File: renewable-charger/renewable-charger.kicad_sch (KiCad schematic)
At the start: 19 parts

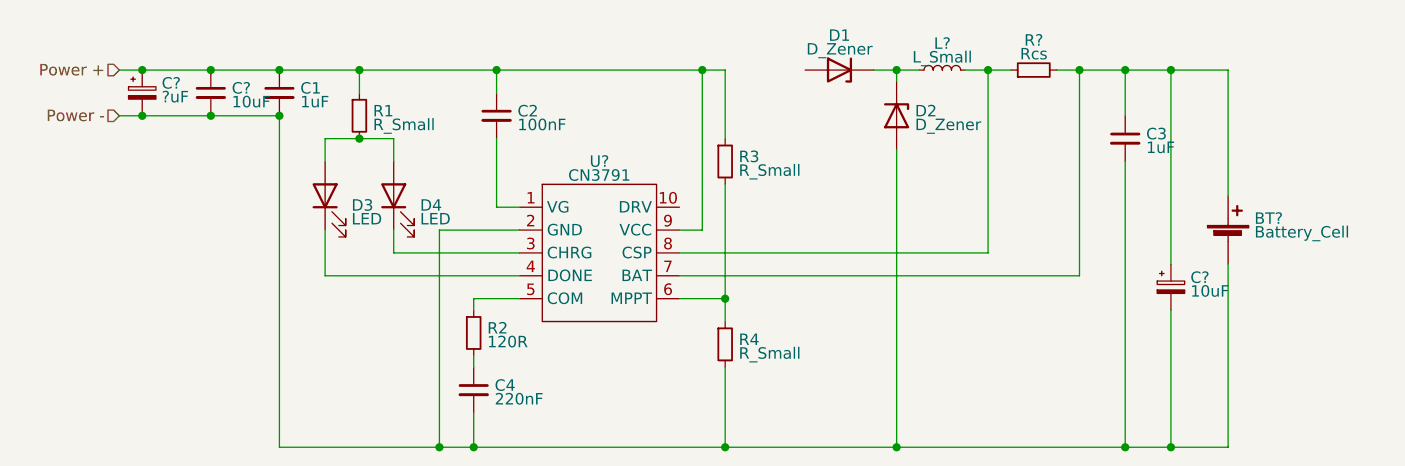
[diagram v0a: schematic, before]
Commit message: Schematic almost finished—most components chosen with part numbers.  Start made on PCB.  Part of #2
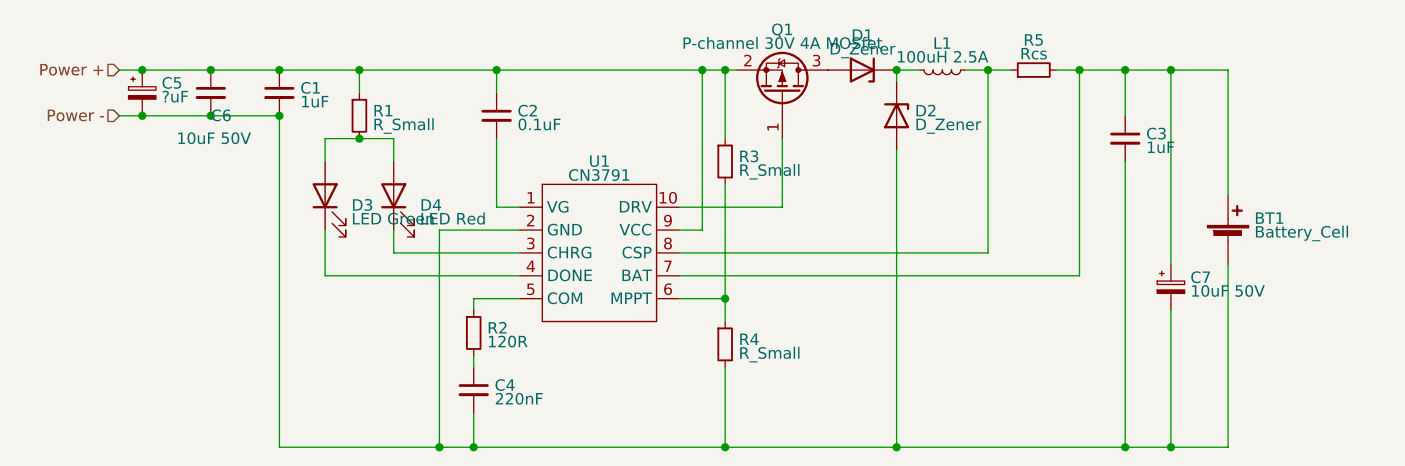
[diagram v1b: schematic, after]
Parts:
- added Q1: P-channel 30V 4A MOSfet, Package_TO_SOT_SMD:SOT-23, symbol Transistor_FET:AO3401A
- BT1: renamed from BT?; footprint (none) -> Connector_JST:JST_PH_S2B-PH-SM4-TB_1x02-1MP_P2.00mm_Horizontal
- C1, C3: footprint (none) -> Capacitor_SMD:C_0603_1608Metric_Pad1.08x0.95mm_HandSolder; Farnell (none) -> 2211179; Farnell Price/Stock (none) -> https://uk.farnell.com/tdk/c1608x5r1h105k080ab/cap-1-f-50v-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
- C2: value 100nF -> 0.1uF; footprint (none) -> Capacitor_SMD:C_0603_1608Metric_Pad1.08x0.95mm_HandSolder; Farnell (none) -> 1759122; Farnell Price/Stock (none) -> https://uk.farnell.com/multicomp/mc0603b104k500ct/cap-0-1-f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
- C4: footprint (none) -> Capacitor_SMD:C_0603_1608Metric_Pad1.08x0.95mm_HandSolder; Farnell (none) -> 2346906; Farnell Price/Stock (none) -> https://uk.farnell.com/tdk/c1608x7r1h224k080ab/cap-0-22-f-5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
- C6, C7: renamed from C?; value 10uF -> 10uF 50V; footprint (none) -> Capacitor_SMD:C_1206_3216Metric_Pad1.33x1.80mm_HandSolder; Farnell (none) -> 3013512; Farnell Price/Stock (none) -> https://uk.farnell.com/samsung-electro-mechanics/cl31a106kb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
- D1, D2: footprint (none) -> Diode_SMD:D_SMF; Farnell (none) -> 3014176; Farnell Price/Stock (none) -> https://uk.farnell.com/vishay/v3fl45hm3-h/schottky-rect-sin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
- D3: value LED -> LED Green; footprint (none) -> LED_SMD:LED_0805_2012Metric_Pad1.15x1.40mm_HandSolder; Farnell (none) -> 3796308; Farnell Price/Stock (none) -> https://uk.farnell.com/multicomp-pro/mp008279/led-green-70m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
- D4: value LED -> LED Red; footprint (none) -> LED_SMD:LED_0805_2012Metric_Pad1.15x1.40mm_HandSolder; Farnell (none) -> 3796325; Farnell Price/Stock (none) -> https://uk.farnell.com/multicomp-pro/mp008293/led-red-220mc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
- L1: renamed from L?; value L_Small -> 100uH 2.5A; footprint (none) -> Inductor_SMD:L_12x12mm_H6mm; Farnell (none) -> 3380989; Farnell Price/Stock (none) -> https://uk.farnell.com/wurth-elektronik/7447706101/inductor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
- R1: footprint (none) -> Resistor_SMD:R_0603_1608Metric_Pad0.98x0.95mm_HandSolder
- R2: footprint (none) -> Resistor_SMD:R_0603_1608Metric_Pad0.98x0.95mm_HandSolder; Farnell (none) -> 2447240; Farnell Price/Stock (none) -> https://uk.farnell.com/multicomp/mcwr06x1200ftl/res-120r-1-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
- R3, R4: footprint (none) -> Resistor_SMD:R_0805_2012Metric_Pad1.20x1.40mm_HandSolder
- R5: renamed from R?; footprint (none) -> Resistor_SMD:R_0805_2012Metric_Pad1.20x1.40mm_HandSolder; Farnell (none) -> 2483502; Farnell Price/Stock (none) -> https://uk.farnell.com/te-connectivity/tlm2aer068jte/curren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
- gave numbers to parts that had none: 2
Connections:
- net Power +: now also Q1.2 (S)
- net at U1.10 (DRV): now also Q1.1 (G)
- net at D1.2 (A): now also Q1.3 (D)
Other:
- moved on the sheet: D1, L1

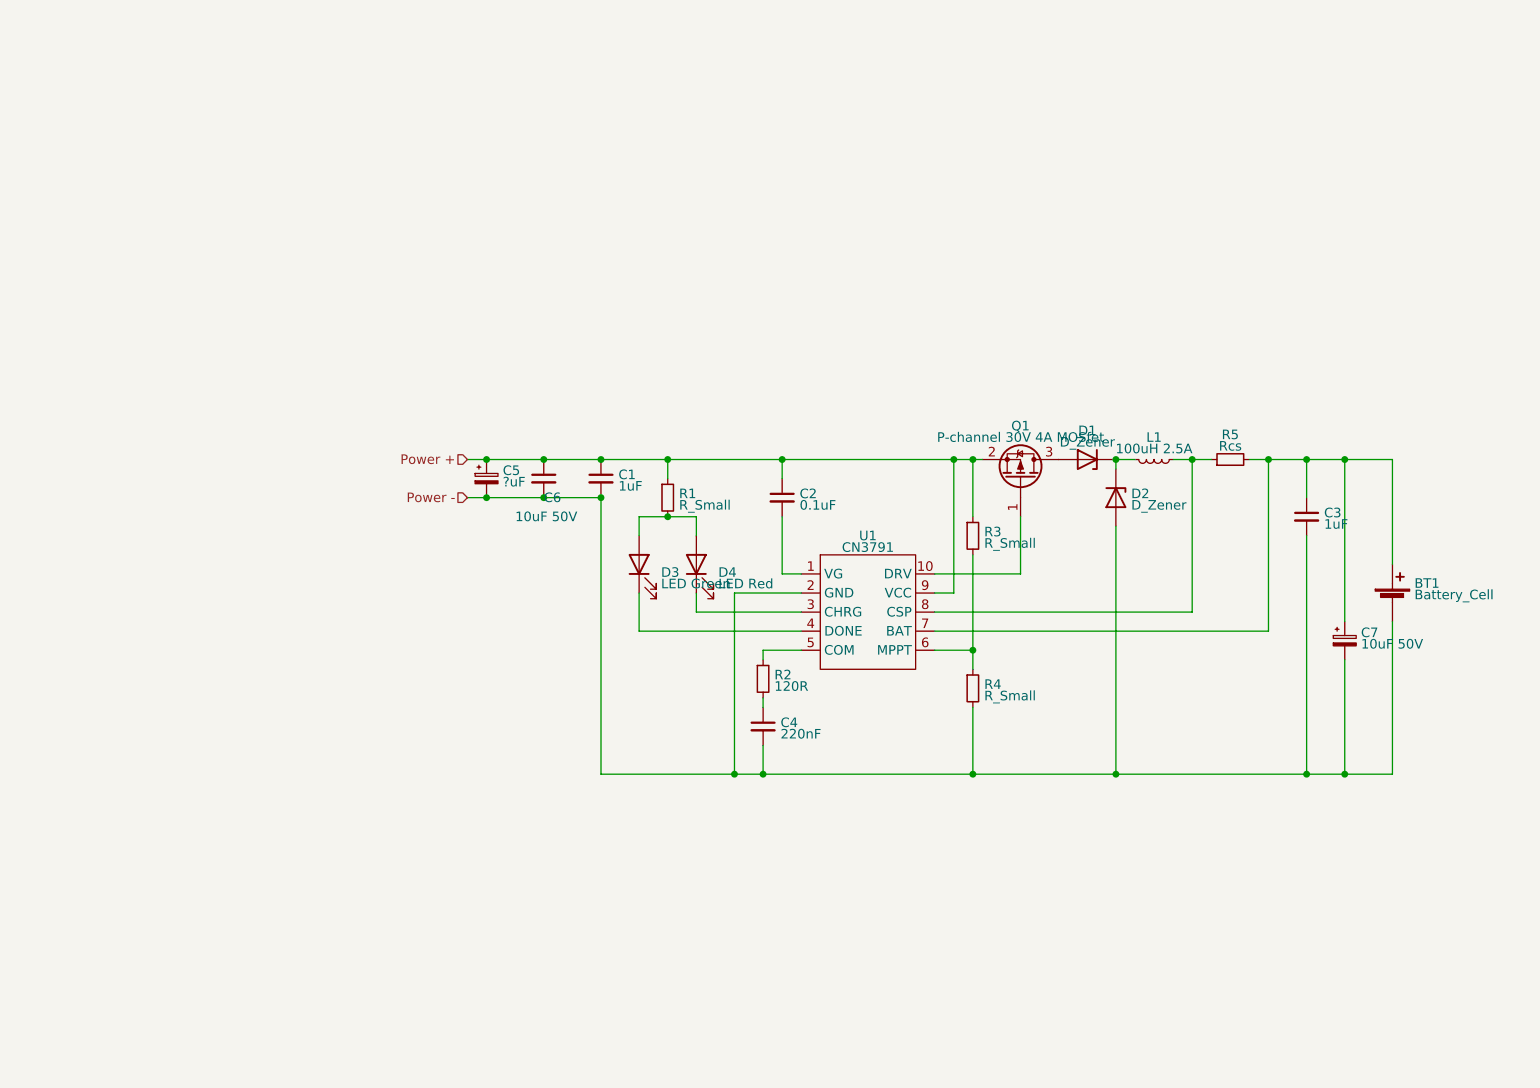
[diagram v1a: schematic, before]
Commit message: Add windmill rectifying voltage-doubler circuit to the schematic.  Part of #6
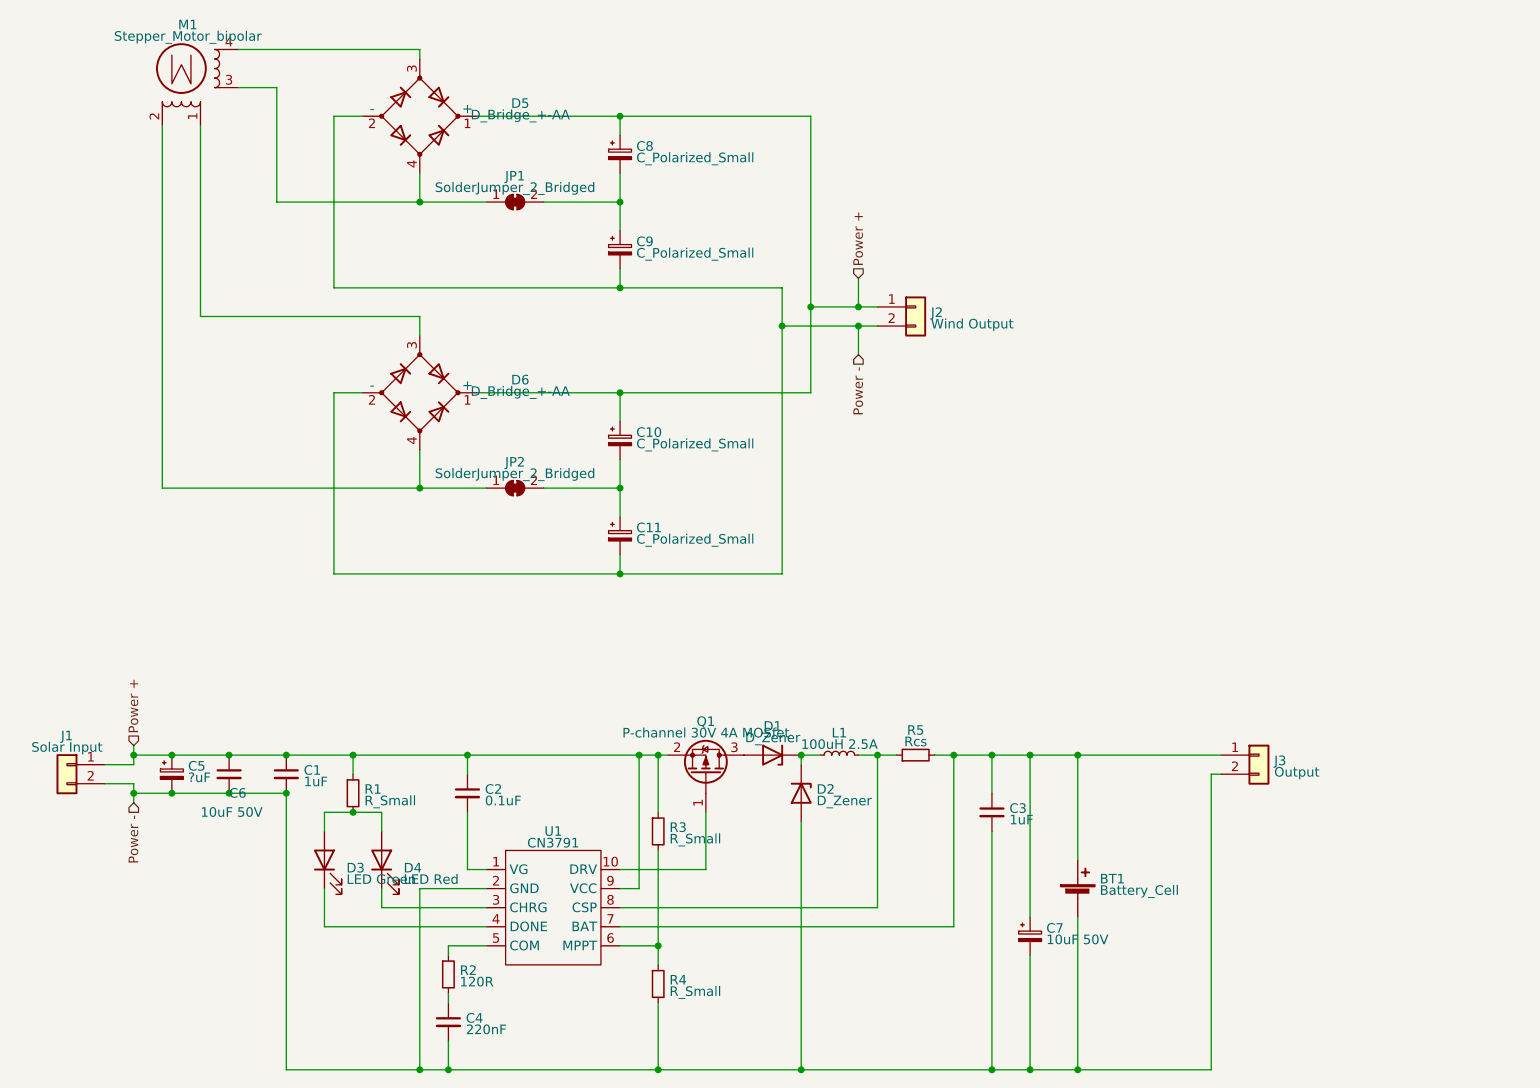
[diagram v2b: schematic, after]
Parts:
- added C10, C11, C8, C9: C_Polarized_Small, Capacitor_SMD:CP_Elec_8x10.5, symbol Device:C_Polarized_Small
- added D5, D6: D_Bridge_+-AA, symbol Device:D_Bridge_+-AA
- added J1: Solar Input, Connector_Phoenix_MSTB:PhoenixContact_MSTBVA_2,5_2-G-5,08_1x02_P5.08mm_Vertical, symbol Connector_Generic:Conn_01x02
- added J2: Wind Output, Connector_Phoenix_MSTB:PhoenixContact_MSTBVA_2,5_2-G-5,08_1x02_P5.08mm_Vertical, symbol Connector_Generic:Conn_01x02
- added J3: Output, Connector_Phoenix_MSTB:PhoenixContact_MSTBVA_2,5_2-G-5,08_1x02_P5.08mm_Vertical, symbol Connector_Generic:Conn_01x02
- added JP1, JP2: SolderJumper_2_Bridged, Jumper:SolderJumper-2_P1.3mm_Bridged_RoundedPad1.0x1.5mm, symbol Jumper:SolderJumper_2_Bridged
- added M1: Stepper_Motor_bipolar, Connector_Phoenix_MSTB:PhoenixContact_MSTBVA_2,5_4-G-5,08_1x04_P5.08mm_Vertical, symbol Motor:Stepper_Motor_bipolar
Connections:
- net Power +: now also C10.1, C8.1, D5.1 (+), D6.1 (+), J1.1 (Pin_1), J2.1 (Pin_1)
- net Power -: now also C11.2, C9.2, D5.2 (-), D6.2 (-), J1.2 (Pin_2), J2.2 (Pin_2), J3.2 (Pin_2)
- net at BT1.1 (+), C3.1, C7.1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: now also J3.1 (Pin_1)
- new net: D6.4, JP2.1 (A), M1.2 (-)
- new net: C10.2, C11.1, JP2.2 (B)
- new net: C8.2, C9.1, JP1.2 (B)
- new net: D5.3, M1.4
- new net: D5.4, JP1.1 (A), M1.3
- new net: D6.3, M1.1
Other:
- title: (none) -> Windmill/Solar Charger
- moved on the sheet: BT1, C1, C2, C3, C4, C5, C6, C7, D1, D2, D3, D4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

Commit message: The windmill rectifier circuit is laid out on the PCB, apart from routing bits to the output connector, as its final location isn't set yet.  Part of #6
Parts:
- D5, D6: footprint (none) -> BridgeRectifier:BridgeRectifier_DBLS
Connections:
- net at D6.4, JP2.1 (A): now also M1.1; no longer M1.2 (-)
- net at D6.3: now also M1.2 (-); no longer M1.1
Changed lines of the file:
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@@
   (junction (at 57.15 132.08) (diameter 0) (color 0 0 0 0)
   )
+  (wire (pts (xy 31.75 40.64) (xy 31.75 66.04))
+    (stroke (width 0) (type default))
+  )
   (wire (pts (xy 54.61 100.33) (xy 92.71 100.33))
     (stroke (width 0) (type default))
@@
     (stroke (width 0) (type default))
   )
-  (wire (pts (xy 31.75 88.9) (xy 31.75 40.64))
-    (stroke (width 0) (type default))
-  )
   (wire (pts (xy 97.79 137.16) (xy 97.79 149.86))
     (stroke (width 0) (type default))
@@
     (stroke (width 0) (type default))
   )
-  (wire (pts (xy 36.83 66.04) (xy 66.04 66.04))
+  (wire (pts (xy 31.75 66.04) (xy 66.04 66.04))
     (stroke (width 0) (type default))
   )
@@
     (stroke (width 0) (type default))
   )
-  (wire (pts (xy 36.83 40.64) (xy 36.83 66.04))
-    (stroke (width 0) (type default))
-  )
   (wire (pts (xy 46.99 50.8) (xy 66.04 50.8))
     (stroke (width 0) (type default))
   )
+  (wire (pts (xy 36.83 40.64) (xy 36.83 88.9))
+    (stroke (width 0) (type default))
+  )
   (wire (pts (xy 142.24 166.37) (xy 147.32 166.37))
     (stroke (width 0) (type default))
@@
     (stroke (width 0) (type default))
   )
-  (wire (pts (xy 66.04 88.9) (xy 31.75 88.9))
+  (wire (pts (xy 66.04 88.9) (xy 36.83 88.9))
     (stroke (width 0) (type default))
   )
@@
       (effects (font (size 1.27 1.27)))
     )
-    (property "Footprint" "" (id 2) (at 66.04 39.37 0)
+    (property "Footprint" "BridgeRectifier:BridgeRectifier_DBLS" (id 2) (at 66.04 39.37 0)
       (effects (font (size 1.27 1.27)) hide)
     )
@@
       (effects (font (size 1.27 1.27)))
     )
-    (property "Footprint" "" (id 2) (at 66.04 76.2 0)
+    (property "Footprint" "BridgeRectifier:BridgeRectifier_DBLS" (id 2) (at 66.04 76.2 0)
       (effects (font (size 1.27 1.27)) hide)
     )
@@
     )
     (path "/5ad39790-bf38-4b96-a574-354746ed74b4"
-      (reference "D5") (unit 1) (value "D_Bridge_+-AA") (footprint "")
+      (reference "D5") (unit 1) (value "D_Bridge_+-AA") (footprint "BridgeRectifier:BridgeRectifier_DBLS")
     )
     (path "/e1a2236e-9438-4cf8-9628-4a2edf553390"
-      (reference "D6") (unit 1) (value "D_Bridge_+-AA") (footprint "")
+      (reference "D6") (unit 1) (value "D_Bridge_+-AA") (footprint "BridgeRectifier:BridgeRectifier_DBLS")
     )
     (path "/05128b57-84e4-4fd9-ad70-96d2e92c0a7b"
